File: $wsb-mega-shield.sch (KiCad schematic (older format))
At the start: 14 parts

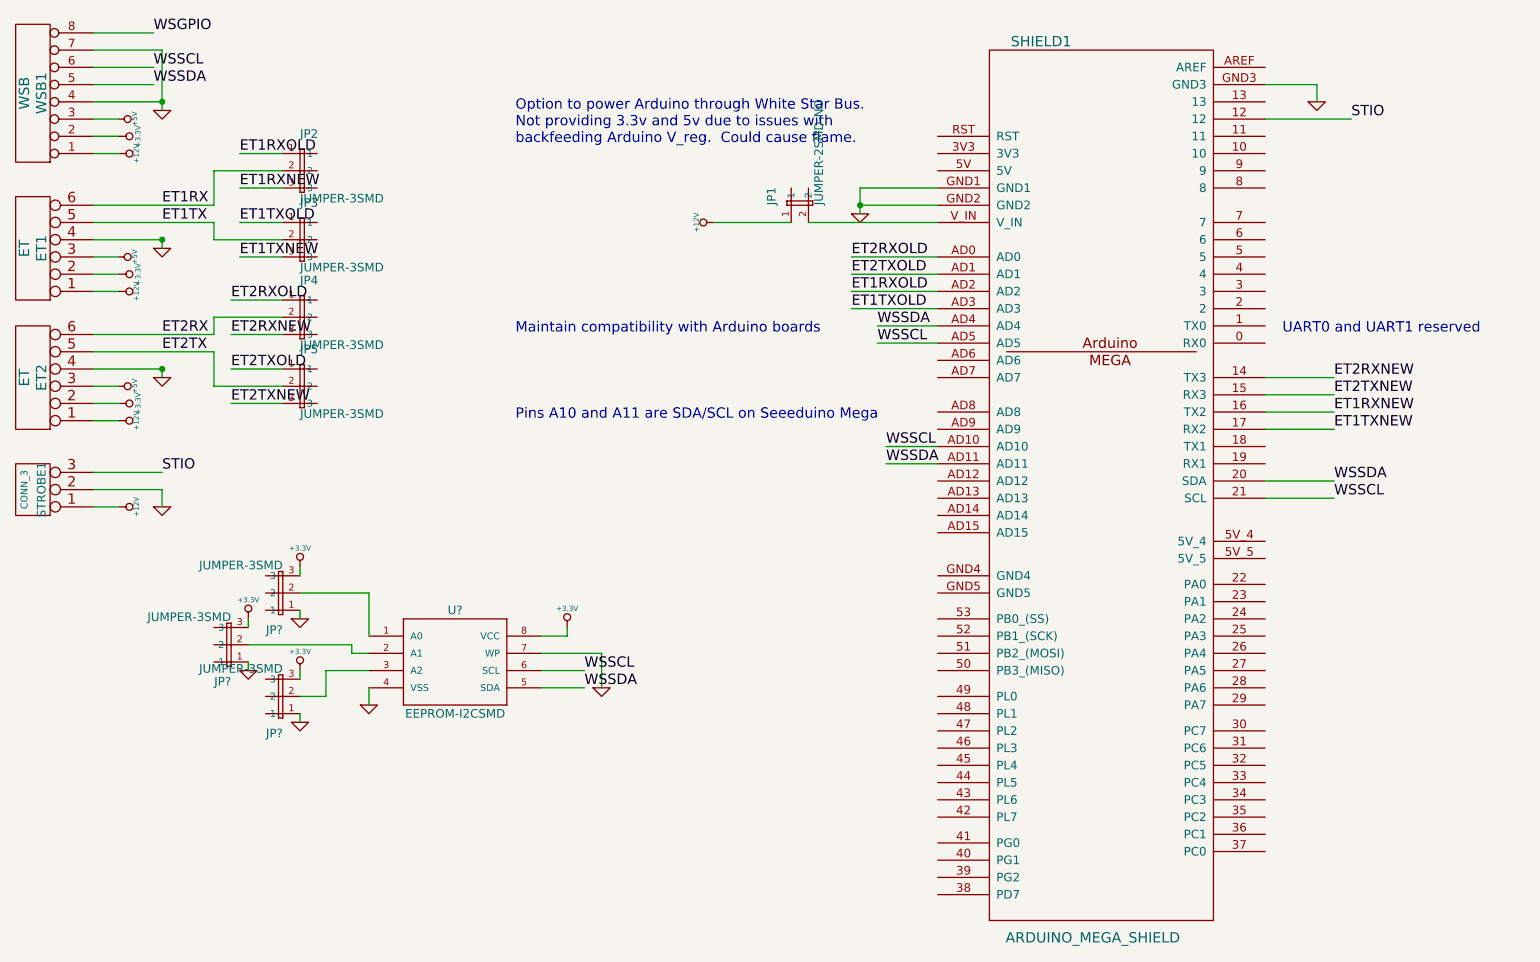
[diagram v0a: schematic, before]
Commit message: Cleaned up silk, added more vias, added eeprom
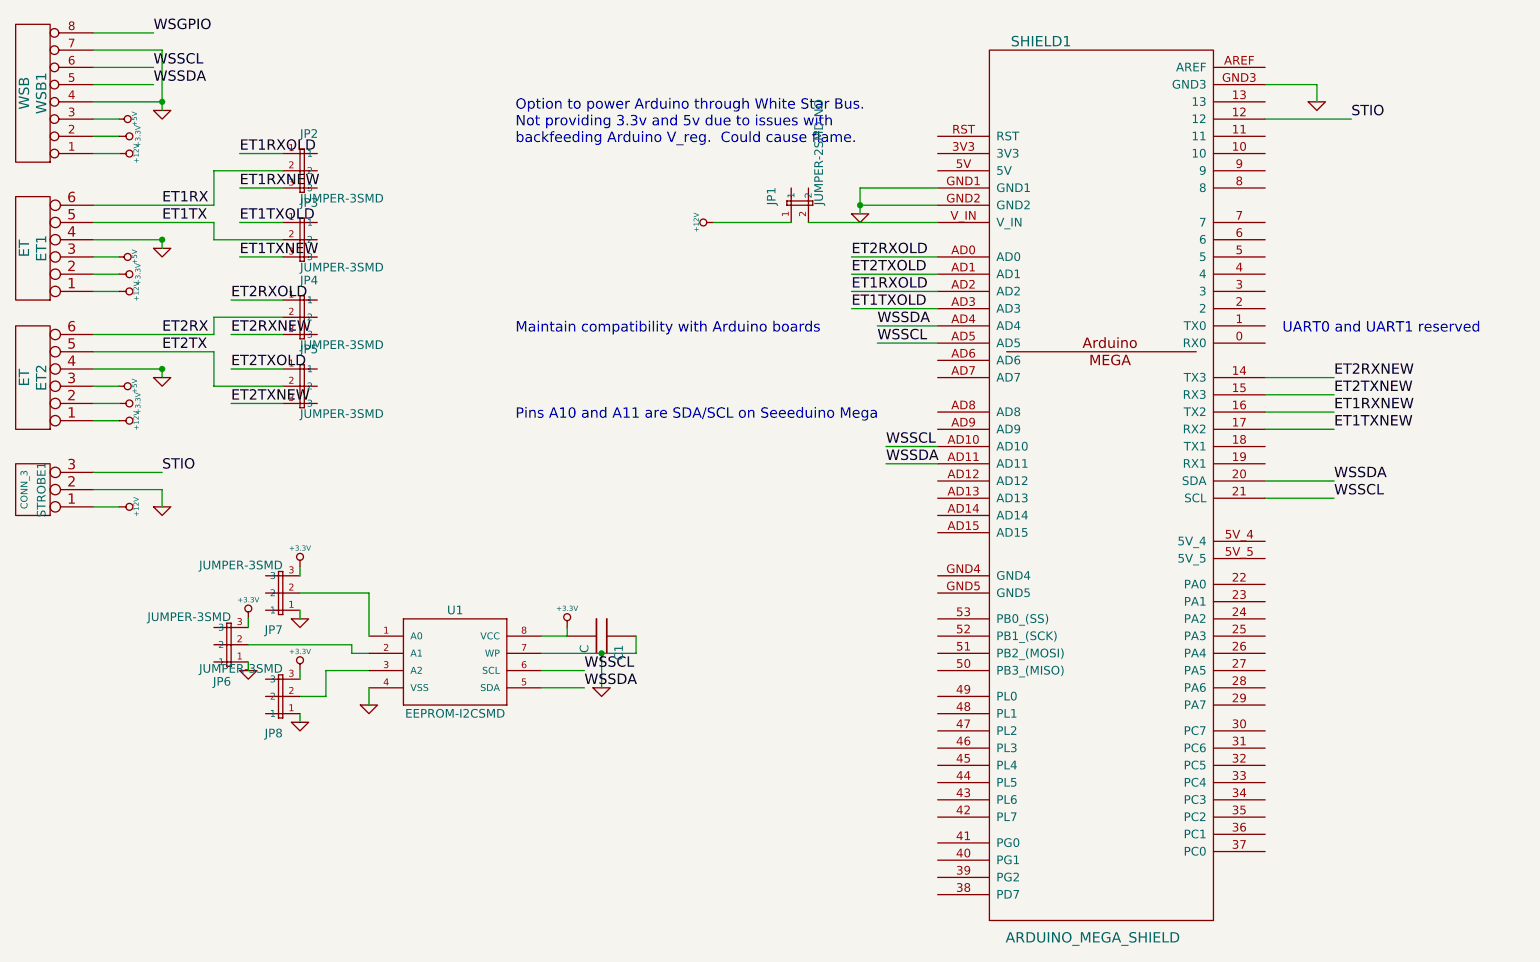
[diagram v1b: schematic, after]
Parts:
- added C1: C, symbol C
- gave numbers to parts that had none: 4
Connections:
- net +3.3V: now also C1.2
- net GND: now also C1.1

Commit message: Relaid board
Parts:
- removed JP1: JUMPER-2SMD-NO, SparkFun-SJ_2S-NO, symbol JUMPER-2SMD-NO
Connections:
- net +12V: now also SHIELD1.V_IN
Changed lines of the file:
@@
-EESchema Schematic File Version 2  date Fri 30 Dec 2011 08:09:24 PM EST
+EESchema Schematic File Version 2  date Fri 30 Dec 2011 11:14:58 PM EST
 LIBS:power
 LIBS:device
@@
 Comment4 ""
 $EndDescr
+Wire Wire Line
+	7100 2450 5800 2450
+Wire Wire Line
+	3400 5200 3550 5200
+Wire Wire Line
+	3550 5200 3550 5050
+Wire Wire Line
+	3550 5050 3800 5050
+Wire Wire Line
+	3400 4600 3800 4600
+Wire Wire Line
+	3800 4600 3800 4850
+Wire Wire Line
+	3400 5300 3400 5350
+Wire Wire Line
+	4800 5050 5050 5050
+Wire Wire Line
+	4950 4800 4950 4850
+Wire Wire Line
+	4950 4850 4800 4850
+Wire Wire Line
+	7100 2950 6600 2950
+Wire Wire Line
+	7100 2750 6600 2750
+Wire Wire Line
+	3300 3500 3000 3500
+Wire Wire Line
+	3300 2900 3000 2900
+Wire Wire Line
+	3300 3000 2900 3000
+Wire Wire Line
+	2900 3000 2900 3100
+Wire Wire Line
+	2900 3100 2200 3100
+Wire Wire Line
+	3300 2650 3050 2650
+Wire Wire Line
+	3300 2450 3050 2450
+Wire Wire Line
+	2200 2350 2900 2350
+Wire Wire Line
+	6750 3150 7100 3150
+Wire Wire Line
+	9000 1850 9500 1850
+Wire Wire Line
+	9000 3350 9400 3350
+Wire Wire Line
+	7100 3850 6800 3850
+Wire Wire Line
+	9000 3950 9400 3950
+Wire Wire Line
+	9000 3650 9400 3650
+Connection ~ 6650 2350
+Wire Wire Line
+	7100 2350 6650 2350
+Wire Wire Line
+	9300 1750 9300 1650
+Wire Wire Line
+	9300 1650 9000 1650
+Wire Wire Line
+	2600 4100 2600 4000
+Wire Wire Line
+	2600 4000 2200 4000
+Connection ~ 2600 3300
+Wire Wire Line
+	2350 3500 2200 3500
+Wire Wire Line
+	2200 3300 2600 3300
+Wire Wire Line
+	2200 3400 2350 3400
+Wire Wire Line
+	2350 3600 2200 3600
+Wire Wire Line
+	2600 3300 2600 3350
+Wire Wire Line
+	2600 2600 2600 2550
+Wire Wire Line
+	2200 1650 2550 1650
+Connection ~ 2600 1750
+Wire Wire Line
+	2600 1800 2600 1450
+Wire Wire Line
+	2600 1450 2200 1450
+Wire Wire Line
+	2350 1950 2200 1950
+Wire Wire Line
+	2600 1750 2200 1750
+Wire Wire Line
+	2200 1850 2350 1850
+Wire Wire Line
+	2350 2050 2200 2050
+Wire Wire Line
+	2200 1550 2550 1550
+Wire Wire Line
+	2200 1350 2550 1350
+Wire Wire Line
+	2350 2850 2200 2850
+Wire Wire Line
+	2200 2650 2350 2650
+Wire Wire Line
+	2600 2550 2200 2550
+Wire Wire Line
+	2350 2750 2200 2750
+Connection ~ 2600 2550
+Wire Wire Line
+	2200 4100 2350 4100
+Wire Wire Line
+	2200 3900 2600 3900
+Wire Wire Line
+	7100 2250 6650 2250
+Wire Wire Line
+	6650 2250 6650 2400
+Wire Wire Line
+	9000 3550 9400 3550
+Wire Wire Line
+	9000 4050 9400 4050
+Wire Wire Line
+	7100 3750 6800 3750
+Wire Wire Line
+	9000 3450 9400 3450
+Wire Wire Line
+	7100 3050 6750 3050
+Wire Wire Line
+	2900 2350 2900 2150
+Wire Wire Line
+	2900 2150 3300 2150
+Wire Wire Line
+	2200 2450 2900 2450
+Wire Wire Line
+	2900 2450 2900 2550
+Wire Wire Line
+	2900 2550 3300 2550
+Wire Wire Line
+	3300 2050 3050 2050
+Wire Wire Line
+	3300 2250 3050 2250
+Wire Wire Line
+	2200 3200 2900 3200
+Wire Wire Line
+	2900 3200 2900 3400
+Wire Wire Line
+	2900 3400 3300 3400
+Wire Wire Line
+	3300 3100 3000 3100
+Wire Wire Line
+	3300 3300 3000 3300
+Wire Wire Line
+	7100 2650 6600 2650
+Wire Wire Line
+	7100 2850 6600 2850
+Wire Wire Line
+	3800 5150 3800 5250
+Wire Wire Line
+	5150 4950 5150 5150
+Wire Wire Line
+	4800 5150 5050 5150
+Wire Wire Line
+	3400 5050 3400 5100
+Wire Wire Line
+	3100 4750 3100 4800
+Wire Wire Line
+	3100 5000 3100 5050
+Wire Wire Line
+	3400 4450 3400 4500
+Wire Wire Line
+	3400 4700 3400 4750
+Wire Wire Line
+	3100 4900 3700 4900
+Wire Wire Line
+	3700 4900 3700 4950
+Wire Wire Line
+	3700 4950 3800 4950
+Wire Wire Line
+	4800 4950 5350 4950
+Wire Wire Line
+	5350 4950 5350 4850
 Connection ~ 5150 4950
-Wire Wire Line
-	5350 4850 5350 4950
-Wire Wire Line
-	5350 4950 4800 4950
-Wire Wire Line
-	3800 4950 3700 4950
-Wire Wire Line
-	3700 4950 3700 4900
-Wire Wire Line
-	3700 4900 3100 4900
-Wire Wire Line
-	3400 4700 3400 4750
-Wire Wire Line
-	3400 4450 3400 4500
-Wire Wire Line
-	3100 5000 3100 5050
-Wire Wire Line
-	3100 4750 3100 4800
-Wire Wire Line
-	3400 5050 3400 5100
-Wire Wire Line
-	4800 5150 5050 5150
-Wire Wire Line
-	5150 4950 5150 5150
-Wire Wire Line
-	3800 5150 3800 5250
-Wire Wire Line
-	6250 2450 5800 2450
-Wire Wire Line
-	7100 2850 6600 2850
-Wire Wire Line
-	7100 2650 6600 2650
-Wire Wire Line
-	3300 3300 3000 3300
-Wire Wire Line
-	3300 3100 3000 3100
-Wire Wire Line
-	3300 3400 2900 3400
-Wire Wire Line
-	2900 3400 2900 3200
-Wire Wire Line
-	2900 3200 2200 3200
-Wire Wire Line
-	3300 2250 3050 2250
-Wire Wire Line
-	3300 2050 3050 2050
-Wire Wire Line
-	3300 2550 2900 2550
-Wire Wire Line
-	2900 2550 2900 2450
-Wire Wire Line
-	2900 2450 2200 2450
-Wire Wire Line
-	3300 2150 2900 2150
-Wire Wire Line
-	2900 2150 2900 2350
-Wire Wire Line
-	7100 3050 6750 3050
-Wire Wire Line
-	9000 3450 9400 3450
-Wire Wire Line
-	7100 3750 6800 3750
-Wire Wire Line
-	9000 4050 9400 4050
-Wire Wire Line
-	9000 3550 9400 3550
-Wire Wire Line
-	6650 2400 6650 2250
-Wire Wire Line
-	6650 2250 7100 2250
-Wire Wire Line
-	2200 3900 2600 3900
-Wire Wire Line
-	2200 4100 2350 4100
-Connection ~ 2600 2550
-Wire Wire Line
-	2350 2750 2200 2750
-Wire Wire Line
-	2200 2550 2600 2550
-Wire Wire Line
-	2200 2650 2350 2650
-Wire Wire Line
-	2350 2850 2200 2850
-Wire Wire Line
-	2200 1350 2550 1350
-Wire Wire Line
-	2200 1550 2550 1550
-Wire Wire Line
-	2350 2050 2200 2050
-Wire Wire Line
-	2200 1850 2350 1850
-Wire Wire Line
-	2600 1750 2200 1750
-Wire Wire Line
-	2350 1950 2200 1950
-Wire Wire Line
-	2200 1450 2600 1450
-Wire Wire Line
-	2600 1450 2600 1800
-Connection ~ 2600 1750
-Wire Wire Line
-	2200 1650 2550 1650
-Wire Wire Line
-	2600 2550 2600 2600
-Wire Wire Line
-	2600 3350 2600 3300
-Wire Wire Line
-	2350 3600 2200 3600
-Wire Wire Line
-	2200 3400 2350 3400
-Wire Wire Line
-	2600 3300 2200 3300
-Wire Wire Line
-	2350 3500 2200 3500
-Connection ~ 2600 3300
-Wire Wire Line
-	2200 4000 2600 4000
-Wire Wire Line
-	2600 4000 2600 4100
-Wire Wire Line
-	9000 1650 9300 1650
-Wire Wire Line
-	9300 1650 9300 1750
-Wire Wire Line
-	7100 2350 6650 2350
-Connection ~ 6650 2350
-Wire Wire Line
-	9000 3650 9400 3650
-Wire Wire Line
-	9000 3950 9400 3950
-Wire Wire Line
-	7100 3850 6800 3850
-Wire Wire Line
-	9000 3350 9400 3350
-Wire Wire Line
-	9000 1850 9500 1850
-Wire Wire Line
-	6750 3150 7100 3150
-Wire Wire Line
-	2900 2350 2200 2350
-Wire Wire Line
-	3300 2450 3050 2450
-Wire Wire Line
-	3300 2650 3050 2650
-Wire Wire Line
-	2200 3100 2900 3100
-Wire Wire Line
-	2900 3100 2900 3000
-Wire Wire Line
-	2900 3000 3300 3000
-Wire Wire Line
-	3300 2900 3000 2900
-Wire Wire Line
-	3300 3500 3000 3500
-Wire Wire Line
-	7100 2750 6600 2750
-Wire Wire Line
-	7100 2950 6600 2950
-Wire Wire Line
-	6350 2450 7100 2450
-Wire Wire Line
-	4800 4850 4950 4850
-Wire Wire Line
-	4950 4850 4950 4800
-Wire Wire Line
-	4800 5050 5050 5050
-Wire Wire Line
-	3400 5300 3400 5350
-Wire Wire Line
-	3800 4850 3800 4600
-Wire Wire Line
-	3800 4600 3400 4600
-Wire Wire Line
-	3800 5050 3550 5050
-Wire Wire Line
-	3550 5050 3550 5200
-Wire Wire Line
-	3550 5200 3400 5200
 $Comp
 L C C1
@@
 	1    0    0    -1
 $EndComp
-$Comp
-L JUMPER-2SMD-NO JP1
-U 1 1 4EFDDE62
-P 6250 2350
-F 0 "JP1" V 6165 2350 50  0000 L BNN
-F 1 "JUMPER-2SMD-NO" V 6440 2350 50  0000 L BNN
-F 2 "SparkFun-SJ_2S-NO" H 6250 2500 50  0001 C CNN
-	1    6250 2350
-	1    0    0    -1
-$EndComp
